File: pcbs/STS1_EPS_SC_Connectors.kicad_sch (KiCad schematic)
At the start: 5 parts, among them J2 Panel Y+, J4 Panel Y-, J5 Panel X+, J6 Panel X-, J7 Panel Z-

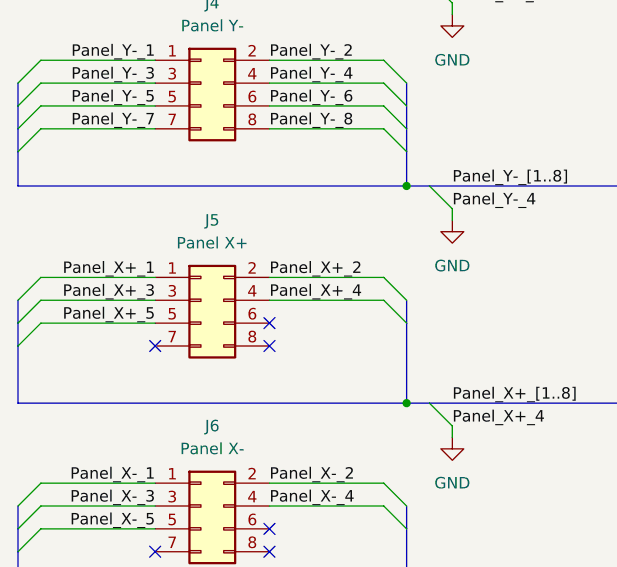
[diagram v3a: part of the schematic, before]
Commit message: Signals to the bus gate should now be provided with supply voltage the proper way.
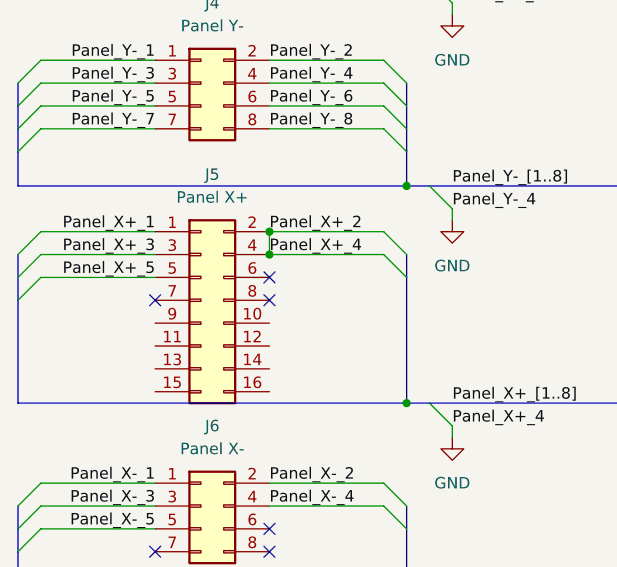
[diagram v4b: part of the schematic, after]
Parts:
- J5: symbol Connector_Generic:Conn_02x04_Odd_Even -> Connector_Generic:Conn_02x08_Odd_Even
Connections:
- net Panel_X+_2 is gone; now on net GND: J5.2 (Pin_2)
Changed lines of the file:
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@@
 	(paper "A4")
+	(junction
+		(at 44.45 64.77)
+		(diameter 0)
+		(color 0 0 0 0)
+	)
 	(junction
 		(at 59.69 83.82)
@@
 		(color 0 0 0 0)
 	)
+	(junction
+		(at 44.45 67.31)
+		(diameter 0)
+		(color 0 0 0 0)
+	)
 	(no_connect
 		(at 31.75 100.33)
@@
 	)
 	(no_connect
-		(at 44.45 74.93)
+		(at 44.45 69.85)
 	)
 	(no_connect
-		(at 44.45 77.47)
+		(at 44.45 72.39)
 	)
 	(no_connect
-		(at 31.75 77.47)
+		(at 31.75 72.39)
 	)
 	(bus_entry
@@
 	)
 	(bus_entry
-		(at 57.15 72.39)
+		(at 57.15 67.31)
 		(size 2.54 2.54)
 		(stroke
@@
 	)
 	(bus_entry
-		(at 19.05 72.39)
+		(at 19.05 67.31)
 		(size -2.54 2.54)
 		(stroke
@@
 	)
 	(bus_entry
-		(at 19.05 74.93)
+		(at 19.05 69.85)
 		(size -2.54 2.54)
 		(stroke
@@
 	)
 	(bus_entry
-		(at 19.05 69.85)
+		(at 19.05 64.77)
 		(size -2.54 2.54)
 		(stroke
@@
 	)
 	(bus_entry
-		(at 57.15 69.85)
+		(at 57.15 64.77)
 		(size 2.54 2.54)
 		(stroke
@@
 	(bus
 		(pts
-			(xy 59.69 72.39) (xy 59.69 74.93)
+			(xy 59.69 67.31) (xy 59.69 69.85)
 		)
 		(stroke
@@
 	(bus
 		(pts
-			(xy 16.51 77.47) (xy 16.51 83.82)
+			(xy 16.51 72.39) (xy 16.51 83.82)
 		)
 		(stroke
@@
 	(wire
 		(pts
-			(xy 19.05 72.39) (xy 31.75 72.39)
+			(xy 19.05 67.31) (xy 31.75 67.31)
 		)
 		(stroke
@@
 	(wire
 		(pts
-			(xy 44.45 72.39) (xy 57.15 72.39)
+			(xy 44.45 67.31) (xy 57.15 67.31)
 		)
 		(stroke
@@
 	(bus
 		(pts
-			(xy 59.69 74.93) (xy 59.69 83.82)
+			(xy 59.69 69.85) (xy 59.69 83.82)
 		)
 		(stroke
@@
 	(wire
 		(pts
+			(xy 44.45 64.77) (xy 44.45 67.31)
+		)
+		(stroke
+			(width 0)
+			(type default)
+		)
+	)
+	(wire
+		(pts
 			(xy 64.77 133.35) (xy 64.77 134.62)
 		)
@@
 	(wire
 		(pts
-			(xy 19.05 74.93) (xy 31.75 74.93)
+			(xy 19.05 69.85) (xy 31.75 69.85)
 		)
 		(stroke
@@
 	(bus
 		(pts
-			(xy 16.51 74.93) (xy 16.51 77.47)
+			(xy 16.51 69.85) (xy 16.51 72.39)
 		)
 		(stroke
@@
 	(wire
 		(pts
-			(xy 44.45 69.85) (xy 57.15 69.85)
+			(xy 44.45 64.77) (xy 57.15 64.77)
 		)
 		(stroke
@@
 	(wire
 		(pts
-			(xy 19.05 69.85) (xy 31.75 69.85)
-		)
-		(stroke
-			(width 0)
-			(type default)
-		)
-	)
-	(bus
-		(pts
-			(xy 16.51 72.39) (xy 16.51 74.93)
+			(xy 19.05 64.77) (xy 31.75 64.77)
+		)
+		(stroke
+			(width 0)
+			(type default)
+		)
+	)
+	(bus
+		(pts
+			(xy 16.51 67.31) (xy 16.51 69.85)
 		)
 		(stroke
@@
 	)
 	(label "Panel_X+_1"
-		(at 31.75 69.85 180)
+		(at 31.75 64.77 180)
 		(fields_autoplaced yes)
 		(effects
@@
 	)
 	(label "Panel_X+_5"
-		(at 31.75 74.93 180)
+		(at 31.75 69.85 180)
 		(fields_autoplaced yes)
 		(effects
@@
 	)
 	(label "Panel_X+_3"
-		(at 31.75 72.39 180)
+		(at 31.75 67.31 180)
 		(fields_autoplaced yes)
 		(effects
@@
 	)
 	(label "Panel_X+_4"
-		(at 44.45 72.39 0)
+		(at 44.45 67.31 0)
 		(fields_autoplaced yes)
 		(effects
@@
 	)
 	(label "Panel_X+_2"
-		(at 44.45 69.85 0)
+		(at 44.45 64.77 0)
 		(fields_autoplaced yes)
 		(effects
@@
 	)
 	(symbol
-		(lib_id "Connector_Generic:Conn_02x04_Odd_Even")
+		(lib_id "Connector_Generic:Conn_02x08_Odd_Even")
 		(at 36.83 72.39 0)
 		(unit 1)
@@
 		(fields_autoplaced yes)
 		(property "Reference" "J5"
-			(at 38.1 63.5 0)
+			(at 38.1 58.42 0)
 			(effects
 				(font
@@
 		)
 		(property "Value" "Panel X+"
-			(at 38.1 66.04 0)
+			(at 38.1 60.96 0)
 			(effects
 				(font
@@
 			)
 		)
-		(property "Description" ""
+		(property "Description" "Generic connector, double row, 02x08, odd/even pin numbering scheme (row 1 odd numbers, row 2 even numbers), script generated (kicad-library-utils/schlib/autogen/connector/)"
 			(at 36.83 72.39 0)
 			(effects
@@
 		(pin "8"
 		)
+		(pin "13"
+		)
+		(pin "11"
+		)
+		(pin "14"
+		)
+		(pin "12"
+		)
+		(pin "16"
+		)
+		(pin "10"
+		)
+		(pin "9"
+		)
+		(pin "15"
+		)
 		(instances

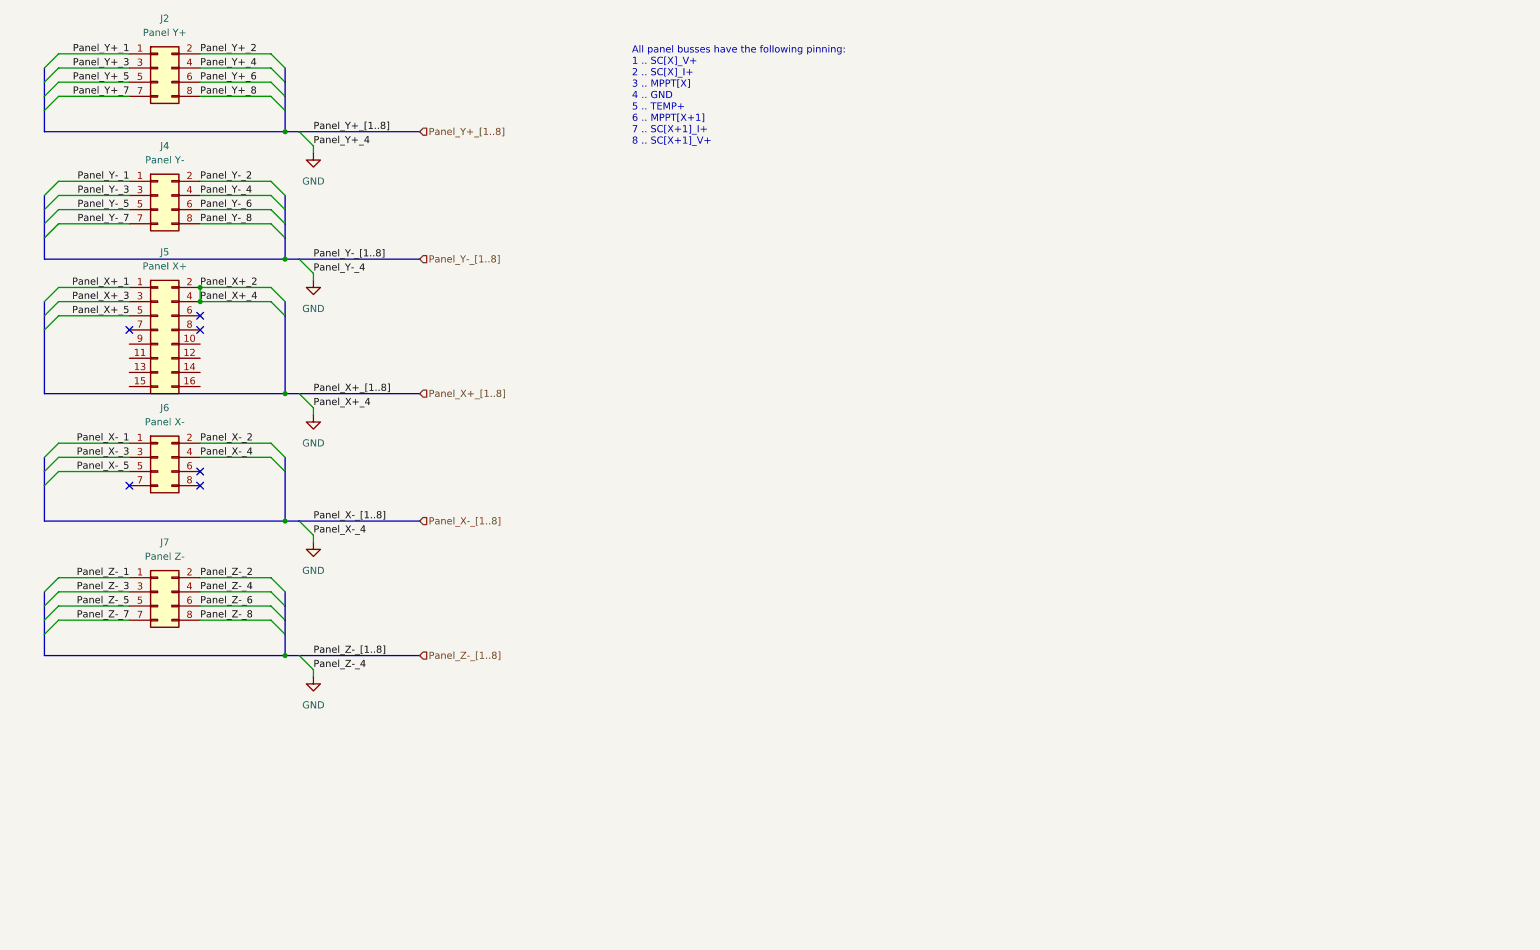
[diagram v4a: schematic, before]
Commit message: Removed UCI connector from STS1_EPS_2 and merged UCI connector with J5 on STS1_EPS_1.
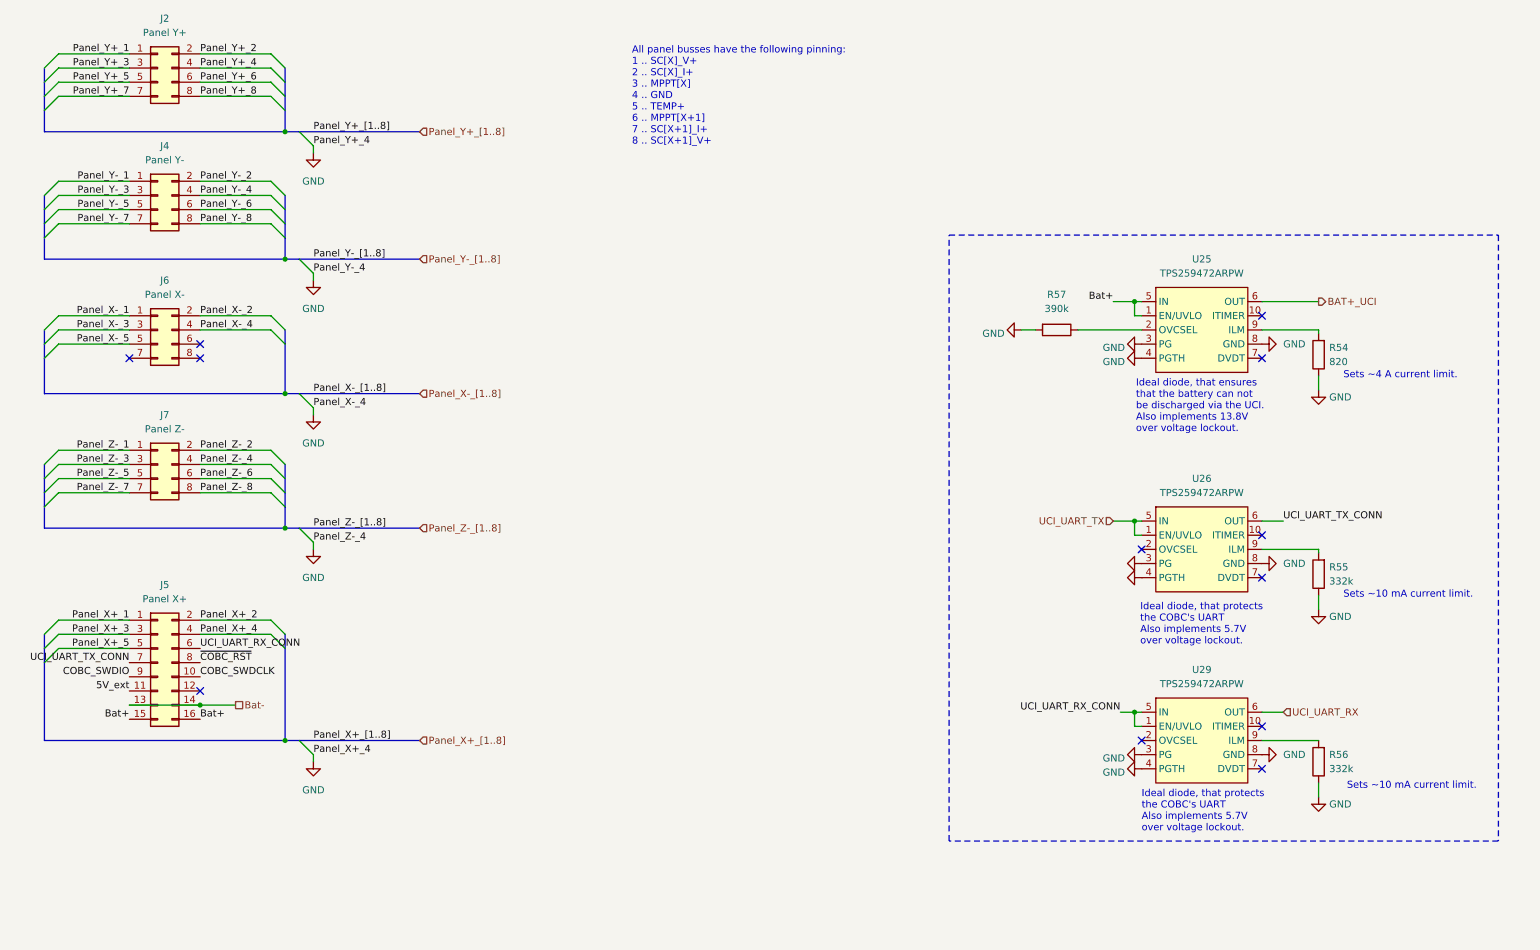
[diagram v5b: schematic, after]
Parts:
- added R54: 820, Resistor_SMD:R_0805_2012Metric, symbol Device:R
- added R55, R56: 332k, Resistor_SMD:R_0805_2012Metric, symbol Device:R
- added R57: 390k, Resistor_SMD:R_0805_2012Metric, symbol Device:R
- added U25, U26, U29: TPS259472ARPW, STS_Package_DFN_QFN:TPS259472ARPWR, symbol STS_Power_Management:TPS259472ARPW
- J5: footprint STS_Connector:SAMTEC_ZF5S-08-03-T-WT -> STS_Connector:SAMTEC_ZF5S-16-03-T-WT
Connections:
- net GND: now also R54.1, R55.1, R56.1, R57.2, U25.3 (PG), U25.4 (PGTH), U25.8 (GND), U26.3 (PG), U26.4 (PGTH), U26.8 (GND), U29.3 (PG), U29.4 (PGTH), U29.8 (GND); no longer J5.2 (Pin_2)
- net COBC_SWDCLK: now reaches J5.10 (Pin_10)
- net 5V_ext: now reaches J5.11 (Pin_11)
- net Bat-: now reaches J5.13 (Pin_13)
- net Bat-: now also J5.14 (Pin_14)
- net Bat+: now reaches J5.15 (Pin_15)
- net Bat+: now also J5.16 (Pin_16), U25.1 (EN/UVLO), U25.5 (IN)
- net UCI_UART_RX_CONN: now reaches J5.6 (Pin_6)
- net UCI_UART_RX_CONN: now also U29.1 (EN/UVLO), U29.5 (IN)
- net UCI_UART_TX_CONN: now reaches J5.7 (Pin_7)
- net UCI_UART_TX_CONN: now also U26.6 (OUT)
- net ~{COBC_RST}: now reaches J5.8 (Pin_8)
- net COBC_SWDIO: now reaches J5.9 (Pin_9)
- new net: R55.2, U26.9 (ILM)
- new net: R56.2, U29.9 (ILM)
- new net: R57.1, U25.2 (OVCSEL)
- new net: R54.2, U25.9 (ILM)
- new net BAT+_UCI: U25.6 (OUT)
- new net Panel_X+_2: J5.2 (Pin_2)
- new net UCI_UART_RX: U29.6 (OUT)
- new net UCI_UART_TX: U26.1 (EN/UVLO), U26.5 (IN)
- no-connect marks 6 -> 12
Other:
- note added: "Ideal diode, that ensures that the battery can not be discharged via the UCI. Also implements 13.8V over voltage lockout."
- note added: "Ideal diode, that protects the COBC's UART Also implements 5.7V over voltage lockout."
- note added: "Sets ~10 mA current limit."
- note added: "Sets ~4 A current limit."
- moved on the sheet: J5, J6, J7

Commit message: Added even more ESD protection.
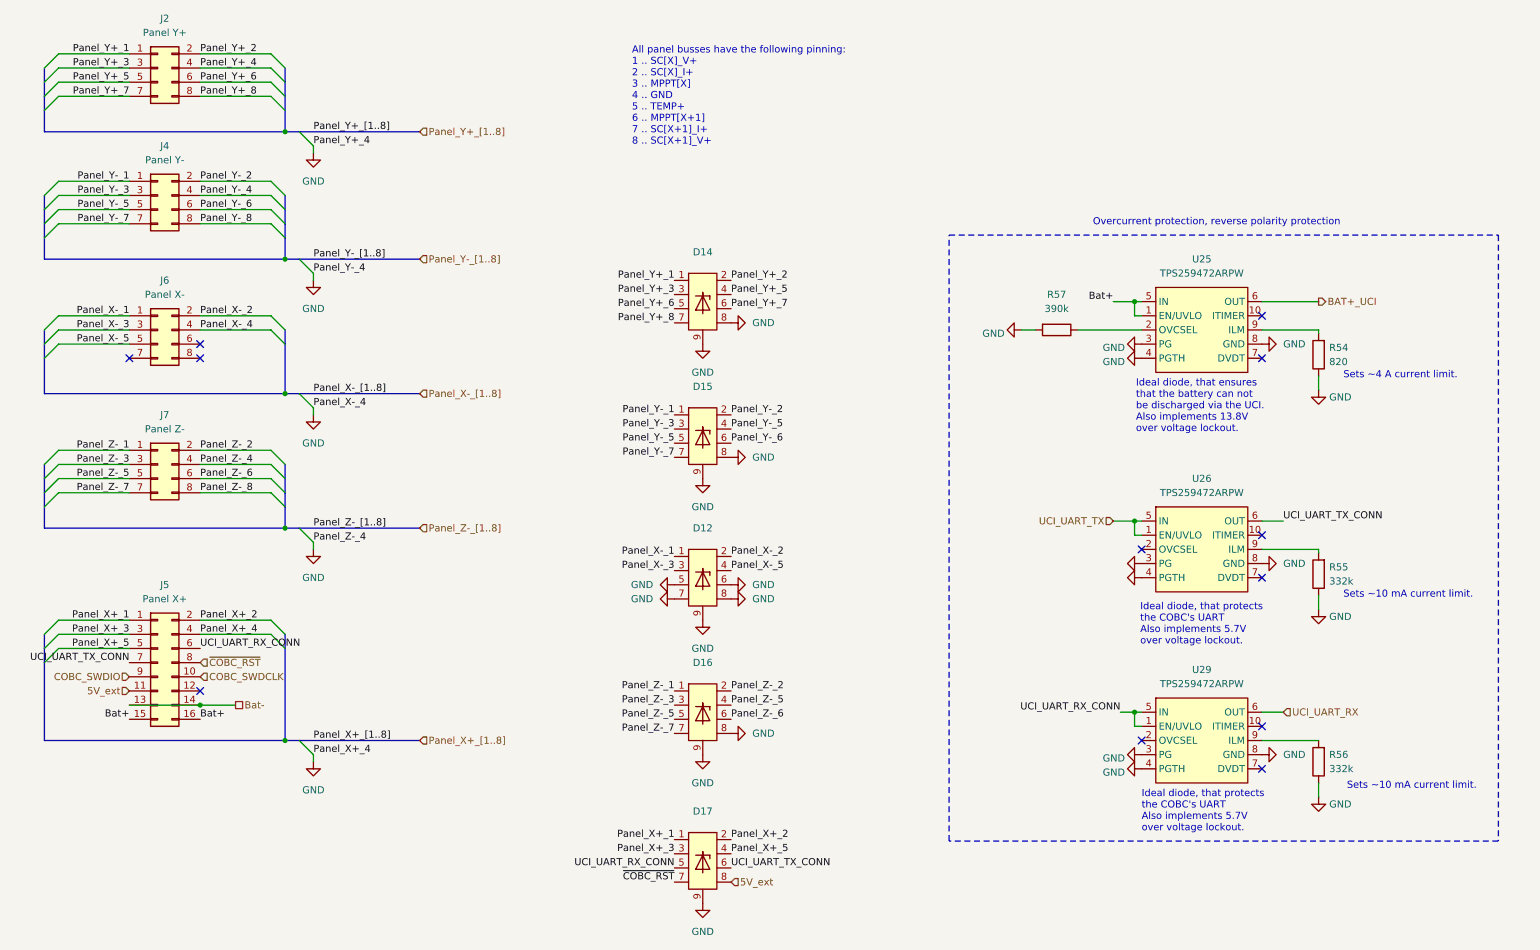
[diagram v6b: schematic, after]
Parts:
- added D12, D14, D15, D16, D17: ~, STS_Misc:LLP1713-9L, symbol STS_Power_Management:VESD05A8A
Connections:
- net 5V_ext: now also D17.8
- net GND: now also D12.5, D12.6, D12.7, D12.8, D12.9, D14.8, D14.9, D15.8, D15.9, D16.8, D16.9, D17.9
- net Panel_X+_1: now also D17.1
- net Panel_X+_2: now also D17.2
- net Panel_X+_3: now also D17.3
- net Panel_X+_5: now also D17.4
- net Panel_X-_1: now also D12.1
- net Panel_X-_2: now also D12.2
- net Panel_X-_3: now also D12.3
- net Panel_X-_5: now also D12.4
- net Panel_Y+_1: now also D14.1
- net Panel_Y+_2: now also D14.2
- net Panel_Y+_3: now also D14.3
- net Panel_Y+_5: now also D14.4
- net Panel_Y+_6: now also D14.5
- net Panel_Y+_7: now also D14.6
- net Panel_Y+_8: now also D14.7
- net Panel_Y-_1: now also D15.1
- net Panel_Y-_2: now also D15.2
- net Panel_Y-_3: now also D15.3
- net Panel_Y-_5: now also D15.4, D15.5
- net Panel_Y-_6: now also D15.6
- net Panel_Y-_7: now also D15.7
- net Panel_Z-_1: now also D16.1
- net Panel_Z-_2: now also D16.2
- net Panel_Z-_3: now also D16.3
- net Panel_Z-_5: now also D16.4, D16.5
- net Panel_Z-_6: now also D16.6
- net Panel_Z-_7: now also D16.7
- net UCI_UART_RX_CONN: now also D17.5
- net UCI_UART_TX_CONN: now also D17.6
- net ~{COBC_RST}: now also D17.7
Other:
- note added: "Overcurrent protection, reverse polarity protection"

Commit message: Reoriented coordinate system.
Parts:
- J2: value Panel Y+ -> Panel Y-
- J4: value Panel Y- -> Panel Y+
- J5: value Panel X+ -> Panel Z-
- J6: value Panel X- -> Panel Z+
- J7: value Panel Z- -> Panel X+
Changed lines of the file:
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@@
 			)
 		)
-		(property "Value" "Panel Z-"
+		(property "Value" "Panel X+"
 			(at 38.1 90.17 0)
 			(effects
@@
 			)
 		)
-		(property "Value" "Panel Y-"
+		(property "Value" "Panel Y+"
 			(at 38.1 41.91 0)
 			(effects
@@
 			)
 		)
-		(property "Value" "Panel Y+"
+		(property "Value" "Panel Y-"
 			(at 38.1 19.05 0)
 			(effects
@@
 			)
 		)
-		(property "Value" "Panel X+"
+		(property "Value" "Panel Z-"
 			(at 38.1 120.65 0)
 			(effects
@@
 			)
 		)
-		(property "Value" "Panel X-"
+		(property "Value" "Panel Z+"
 			(at 38.1 66.04 0)
 			(effects
